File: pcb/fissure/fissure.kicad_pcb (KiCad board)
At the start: 2 copper layers, 151.2 x 81.6 mm, 84 parts, among them J1 AudioJack4, J2 AudioJack4, J3 Conn_01x08, J4 Conn_01x08, J5 Conn_01x08, J6 Conn_01x08, J9 Conn_01x04, K1 KEYSW, K10 KEYSW, K11 KEYSW, K12 KEYSW, K13 KEYSW, K14 KEYSW, K15 KEYSW, K16 KEYSW, K17 KEYSW, K18 KEYSW, K19 KEYSW, K2 KEYSW, K20 KEYSW, K3 KEYSW, K4 KEYSW, K5 KEYSW, K6 KEYSW, K7 KEYSW, K8 KEYSW, K9 KEYSW, SW1 SW_PUSH, SW2 SW_PUSH, U1 ProMicro, U2 MT25QL128ABA1ESE

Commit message: Clean up design files
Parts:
- D1, D10, D11, D12, D13, D14, D15, D16, D17, D18, D19, D2, D20, D21, D22, D23, D24, D25, D26, D27, D28, D29, D3, D30, D31, D32, D33, D34, D35, D36, D37, D38, D39, D4, D40, D5, D6, D7, D8, D9: value DIODE -> D
- J5: renamed from J9; value Conn_01x04 -> OLED
- K1, K10, K11, K12, K13, K14, K15, K16, K17, K18, K19, K2, K20, K3, K4, K5, K6, K7, K8, K9: value KEYSW -> SW_Push
- R1, R2: value R -> 4.7k
- R3: value R -> 10k
- SW1, SW2: value SW_PUSH -> SW_Push
- renumbered J4 to J3, J6 to J4, J3 to J6, J5 to J7
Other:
- outline, holes or cut-outs redrawn

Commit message: update pcb
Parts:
- removed J1: AudioJack4, Keebio-Parts:TRRS-PJ-320D
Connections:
- J4 pad 5: Net-(J4-Pad5) -> bridge_SCL
- J4 pad 6: Net-(J4-Pad6) -> bridge_SDA
- J4 pad 7: Net-(J4-Pad7) -> bridge_VCC
- J4 pad 8: Net-(J4-Pad8) -> bridge_GND
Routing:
- net bridge_GND: track 62.2 -> 72.5 mm
- net bridge_SCL: track 61.7 -> 67.1 mm
- net bridge_SDA: track 62.9 -> 64.5 mm, vias 2 -> 1
- net Net-(J3-Pad2): track 27.6 -> 29.1 mm
- net Net-(J3-Pad3): track 34.0 -> 35.0 mm
- net bridge_VCC: vias 2 -> 1

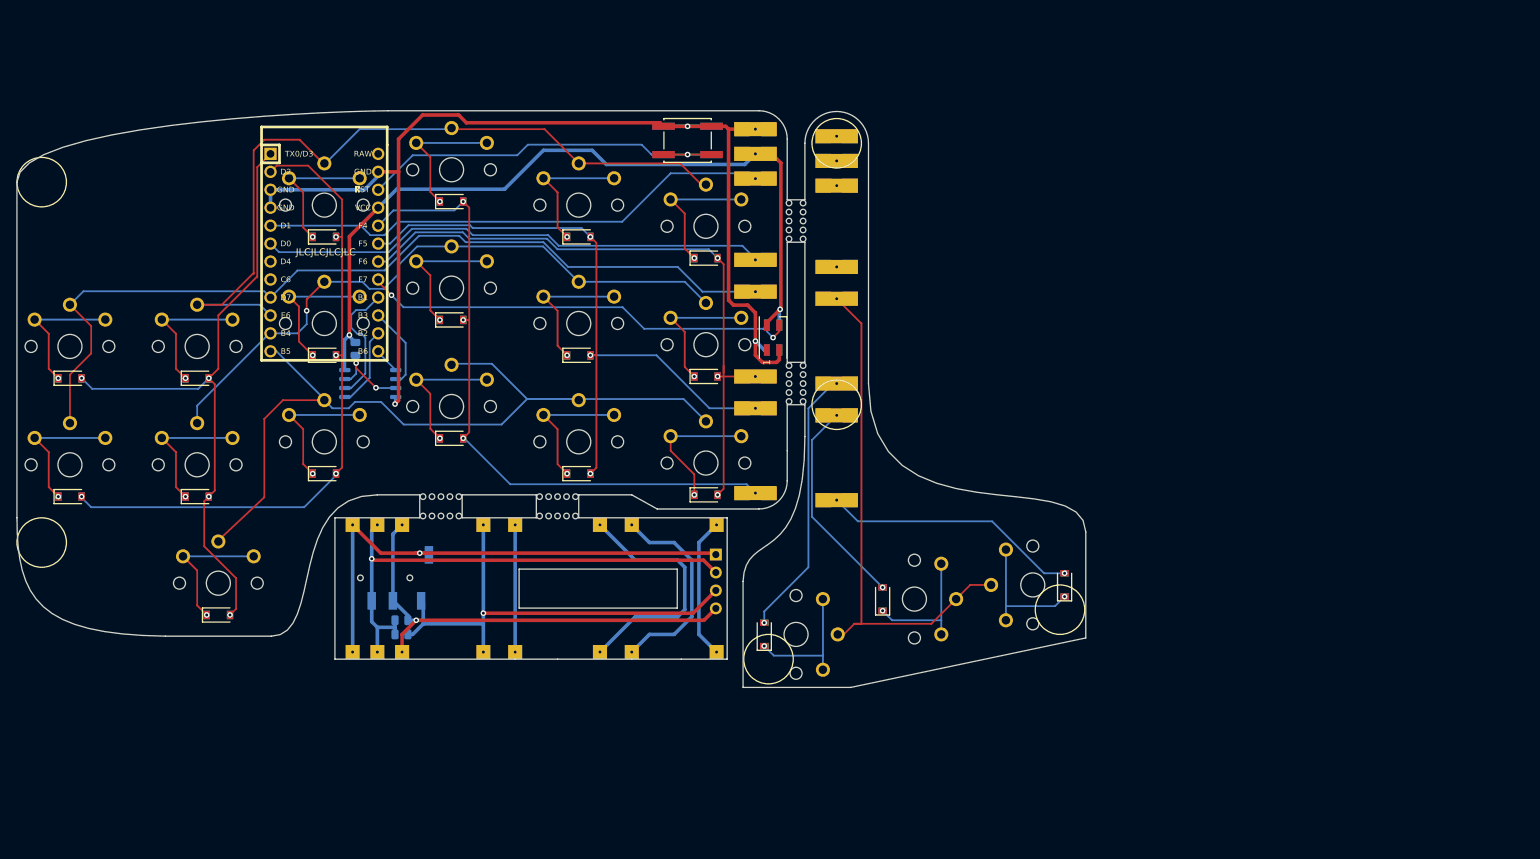
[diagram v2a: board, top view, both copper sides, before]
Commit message: Use new switch footprint
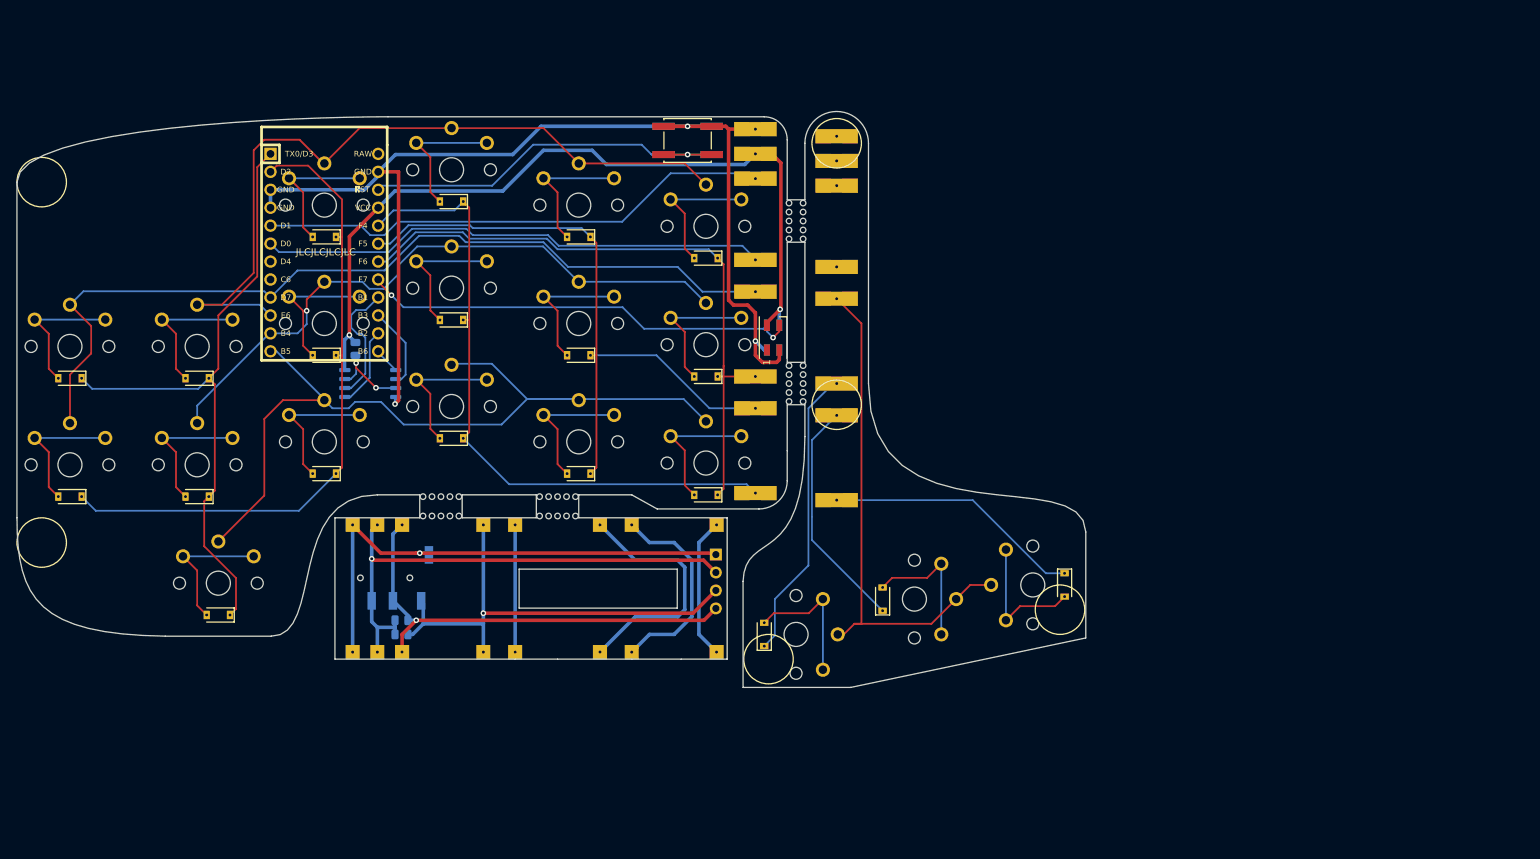
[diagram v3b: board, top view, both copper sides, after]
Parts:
- removed D1, D10, D11, D12, D13, D14, D15, D16, D17, D18, D19, D2, D20, D21, D22, D23, D24, D25, D26, D27, D28, D29, D3, D30, D31, D32, D33, D34, D35, D36, D37, D38, D39, D4, D40, D5, D6, D7, D8, D9: D, Diode_SMD:D_SOD-123
- K1, K10, K11, K12, K13, K14, K15, K16, K17, K2, K3, K4, K5, K6, K7, K8, K9: value SW_Push -> PG1350; footprint Keebio-Parts:Kailh-PG1350-1u-reversible-No-Clickhole -> pg1350:PG1350-reversible-rev
- K18, K19, K20: value SW_Push -> PG1350; footprint Keebio-Parts:Kailh-PG1350-1u-reversible-No-Clickhole -> pg1350:PG1350-reversible-rev; moved to F.Cu
- moved K1 4.50 mm to (51.5, 92.2), turned to 0 degrees
- moved K10 4.50 mm to (123.5, 92.0), turned to 0 degrees
- moved K11 4.50 mm to (54.5, 125.8), turned to 0 degrees
- moved K12 4.50 mm to (69.5, 105.8), turned to 0 degrees
- moved K13 4.50 mm to (87.5, 100.8), turned to 0 degrees
- moved K14 4.50 mm to (105.5, 105.8), turned to 0 degrees
- moved K15 4.50 mm to (123.5, 108.8), turned to 0 degrees
- moved K16 4.50 mm to (33.5, 92.2), turned to 0 degrees
- moved K17 4.50 mm to (33.5, 109.0), turned to 0 degrees
- moved K18 4.50 mm to (174.2, 121.5)
- moved K19 4.50 mm to (148.5, 123.5)
- moved K2 4.50 mm to (69.5, 72.2), turned to 0 degrees
- moved K20 4.50 mm to (131.8, 128.5)
- moved K3 4.50 mm to (87.5, 67.2), turned to 0 degrees
- moved K4 4.50 mm to (105.5, 72.2), turned to 0 degrees
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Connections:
- K1 pad 2: Net-(D1-Pad1) -> COL1
- K10 pad 2: Net-(D19-Pad1) -> COL5
- K11 pad 2: Net-(D21-Pad1) -> COL1
- K12 pad 2: Net-(D23-Pad1) -> COL2
- K13 pad 2: Net-(D25-Pad1) -> COL3
- K14 pad 2: Net-(D27-Pad1) -> COL4
- K15 pad 2: Net-(D29-Pad1) -> COL5
- K16 pad 2: Net-(D31-Pad1) -> COL1
- K17 pad 2: Net-(D33-Pad1) -> COL2
- K18 pad 2: Net-(D35-Pad1) -> thumb_COL3
- K19 pad 2: Net-(D37-Pad1) -> thumb_COL4
- K2 pad 2: Net-(D3-Pad1) -> COL2
- K20 pad 2: Net-(D39-Pad1) -> thumb_COL5
- K3 pad 2: Net-(D5-Pad1) -> COL3
- K4 pad 2: Net-(D7-Pad1) -> COL4
- K5 pad 2: Net-(D10-Pad1) -> COL5
- K6 pad 2: Net-(D11-Pad1) -> COL1
- K7 pad 2: Net-(D13-Pad1) -> COL2
- K8 pad 2: Net-(D15-Pad1) -> COL3
- K9 pad 2: Net-(D17-Pad1) -> COL4
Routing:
- net Net-(D33-Pad1): track 19.7 -> 0.00 mm, vias 1 -> 0
- net Net-(D31-Pad1): track 19.7 -> 0.00 mm, vias 1 -> 0
- net Net-(D21-Pad1): track 19.7 -> 0.00 mm, vias 1 -> 0
- net Net-(D11-Pad1): track 19.7 -> 0.00 mm, vias 1 -> 0
- net Net-(D1-Pad1): track 19.7 -> 0.00 mm, vias 1 -> 0
- net Net-(D7-Pad1): track 19.7 -> 0.00 mm, vias 1 -> 0
- net Net-(D5-Pad1): track 19.7 -> 0.00 mm, vias 1 -> 0
- net Net-(D3-Pad1): track 19.7 -> 0.00 mm, vias 1 -> 0
- net Net-(D29-Pad1): track 19.7 -> 0.00 mm, vias 1 -> 0
- net Net-(D27-Pad1): track 19.7 -> 0.00 mm, vias 1 -> 0
- net Net-(D25-Pad1): track 19.7 -> 0.00 mm, vias 1 -> 0
- net Net-(D23-Pad1): track 19.7 -> 0.00 mm, vias 1 -> 0
- net Net-(D19-Pad1): track 19.7 -> 0.00 mm, vias 1 -> 0
- net Net-(D17-Pad1): track 19.7 -> 0.00 mm, vias 1 -> 0
- net Net-(D15-Pad1): track 19.7 -> 0.00 mm, vias 1 -> 0
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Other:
- board size 151.2 x 81.6 mm -> 151.2 x 81.5 mm

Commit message: Use holyiot 18010 + USB C
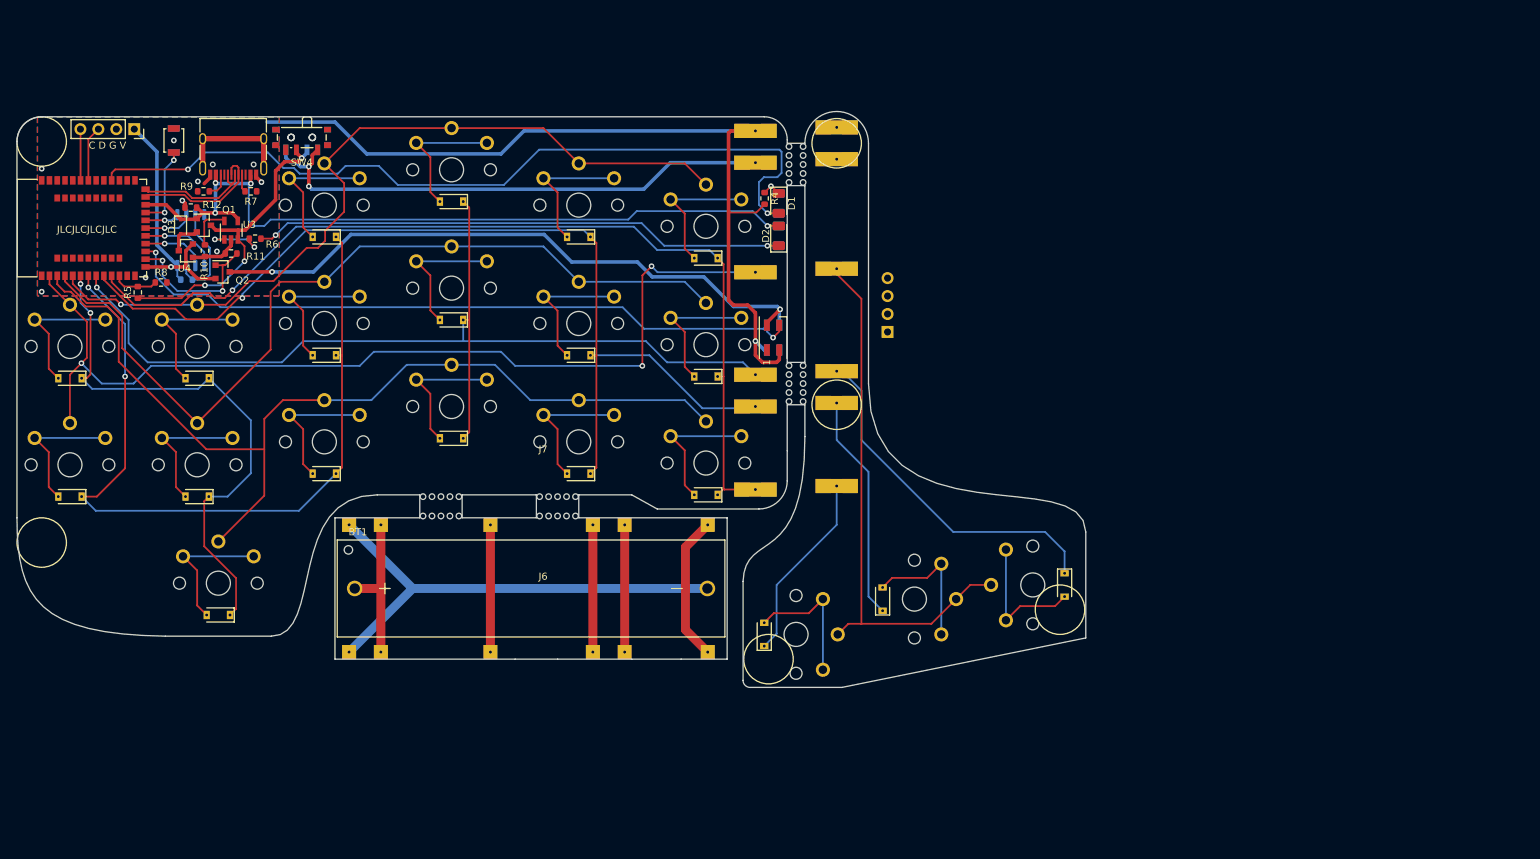
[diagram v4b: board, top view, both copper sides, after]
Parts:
- removed R1, R2: 4.7k, Resistor_SMD:R_0805_2012Metric
- removed the REF** at (137.5, 70.0)
- removed the REF** at (135.0, 70.0)
- added BT1: Battery_Cell, misc:BA1AAAPC, F.Cu at (98.8, 122.0)
- added D1: BLUE, LED_SMD:LED_1206_3216Metric, F.Cu at (133.8, 67.5)
- added D2: RED, LED_SMD:LED_1206_3216Metric, F.Cu at (133.8, 72.1)
- added D3: 1N5819, Diode_SMD:D_SOD-323, F.Cu at (49.1, 70.8)
- added D4: BLUE, LED_SMD:LED_1206_3216Metric, B.Cu at (133.8, 67.5)
- added D5: RED, LED_SMD:LED_1206_3216Metric, B.Cu at (133.8, 72.1)
- added J1: Conn_01x04_Female, Connector_PinSocket_2.54mm:PinSocket_1x04_P2.54mm_Vertical, F.Cu at (42.6, 57.0)
- added Q1: AO3401A, Package_TO_SOT_SMD:SOT-23, F.Cu at (52.5, 70.6)
- added Q2: AO3401A, Package_TO_SOT_SMD:SOT-23, F.Cu at (55.1, 77.2)
- added R10: 10k, Resistor_SMD:R_0603_1608Metric, F.Cu at (52.6, 74.2)
- added R11: 2M, Resistor_SMD:R_0603_1608Metric, F.Cu at (56.3, 74.6)
- added R12: 100k, Resistor_SMD:R_0603_1608Metric, F.Cu at (50.6, 68.1)
- added R4: 1k, Resistor_SMD:R_0603_1608Metric, F.Cu at (131.8, 66.8)
- added R5: 820k, Resistor_SMD:R_0603_1608Metric, F.Cu at (43.1, 80.1)
- added R6: 1k, Resistor_SMD:R_0603_1608Metric, F.Cu at (59.7, 72.5)
- added R7: 5.1k, Resistor_SMD:R_0603_1608Metric, F.Cu at (59.1, 65.8)
- added R8: 2M, Resistor_SMD:R_0603_1608Metric, F.Cu at (46.4, 78.7)
- added R9: 5.1k, Resistor_SMD:R_0603_1608Metric, F.Cu at (52.4, 65.8)
- added REF**: breakaway-mousebites, Keebio-Parts:breakaway-mousebites, F.Cu at (137.5, 62.0)
- added REF**: breakaway-mousebites, Keebio-Parts:breakaway-mousebites, F.Cu at (135.0, 62.0)
- added SW3: SW_SPDT, Button_Switch_SMD:SW_SPDT_PCM12, B.Cu at (66.3, 58.5)
- added SW4: SW_SPDT, Button_Switch_SMD:SW_SPDT_PCM12, F.Cu at (66.3, 58.5)
- added U3: LTC4054ES5-4.2, Package_TO_SOT_SMD:TSOT-23-5, F.Cu at (56.3, 71.3)
- added U4: MCP1700-3302E_SOT23, Package_TO_SOT_SMD:SOT-23, F.Cu at (49.9, 74.2)
- J2: value AudioJack4 -> USB_C_Receptacle_USB2.0; footprint Keebio-Parts:TRRS-PJ-320D -> Connector_USB:USB_C_Receptacle_HRO_TYPE-C-31-M-12; moved to F.Cu
- J3, J4: value Conn_01x08 -> Conn_01x06; footprint fissure:bridge -> fissure:bridge-conn
- J5: footprint steno:OLED -> misc:OLED
- J6: value Conn_01x08 -> Conn_01x06; footprint fissure:bridge-conn -> fissure:bridge
- J7: value Conn_01x08 -> Conn_01x06; footprint fissure:bridge-conn -> fissure:bridge; moved to F.Cu
- R3: footprint Resistor_SMD:R_0805_2012Metric -> Resistor_SMD:R_0603_1608Metric
- SW1, SW2: footprint Button_Switch_SMD:SW_SPST_EVQQ2 -> Button_Switch_SMD:SW_SPST_B3U-1000P
- U1: value ProMicro -> Holyiot_18010; footprint Keebio-Parts:ArduinoProMicro -> misc:Holyiot_18010
- moved SW1 72.7 mm to (48.2, 58.6), turned to 90 degrees
- moved SW2 72.7 mm to (48.2, 58.6), turned to 90 degrees
- moved J2 63.3 mm to (56.6, 59.4), turned to 180 degrees
- moved J6 55.5 mm to (100.2, 131.0), turned to 180 degrees
- moved J5 55.3 mm to (147.6, 75.9), turned to 0 degrees
- moved J3 55.1 mm to (130.5, 84.5), turned to 90 degrees
- moved J4 50.2 mm to (142.0, 84.0), turned to 90 degrees
- moved J7 50.0 mm to (100.2, 113.0), turned to 180 degrees
- moved U1 34.5 mm to (35.2, 71.0), turned to 90 degrees
- moved U2 32.5 mm to (50.6, 72.7), turned to 270 degrees
- moved R3 25.8 mm to (50.0, 78.3), turned to 0 degrees
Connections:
- net RAW renamed Net-(U1-Pad24)
- D41 pad 4: VCC -> EXT_VCC
- D42 pad 4: VCC -> EXT_VCC
- J3 pad 1: Net-(J3-Pad1) -> GND
- J3 pad 2: Net-(J3-Pad2) -> BAT
- J3 pad 3: Net-(J3-Pad3) -> ROW4
- J3 pad 4: Net-(J3-Pad4) -> COL3
- J3 pad 5: bridge_SCL -> COL4
- J3 pad 6: bridge_SDA -> COL5
- J4 pad 1: Net-(J3-Pad1) -> thumb_GND
- J4 pad 2: Net-(J3-Pad2) -> thumb_BAT
- J4 pad 3: Net-(J3-Pad3) -> thumb_ROW4
- J4 pad 4: Net-(J3-Pad4) -> thumb_COL3
- J4 pad 5: bridge_SCL -> thumb_COL4
- J4 pad 6: bridge_SDA -> thumb_COL5
- J5 pad 1: bridge_GND -> GND
- J5 pad 2: bridge_VCC -> EXT_VCC
- J5 pad 3: bridge_SCL -> SCL
- J5 pad 4: bridge_SDA -> SDA
- J6 pad 1: COL3 -> bridge_GND
- J6 pad 2: COL4 -> bridge_BAT
- J6 pad 3: COL5 -> Net-(J6-Pad3)
- J6 pad 4: ROW4 -> Net-(J6-Pad4)
- J6 pad 5: SCL -> Net-(J6-Pad5)
- J6 pad 6: SDA -> Net-(J6-Pad6)
- J7 pad 1: thumb_COL3 -> bridge_GND
- J7 pad 2: thumb_COL4 -> bridge_BAT
- J7 pad 3: thumb_COL5 -> Net-(J6-Pad3)
- J7 pad 4: thumb_ROW4 -> Net-(J6-Pad4)
- J7 pad 5: thumb_SCL -> Net-(J6-Pad5)
- J7 pad 6: thumb_SDA -> Net-(J6-Pad6)
- R3 pad 1: VCC -> VDD
- U1 pad 1: COL1 -> GND
- U1 pad 10: ROW1 -> COL5
- U1 pad 11: ROW2 -> BAT_MEAS
- U1 pad 12: ROW3 -> Net-(U1-Pad12)
- U1 pad 13: CS -> Net-(U1-Pad13)
- U1 pad 14: MOSI_DQ0 -> Net-(U1-Pad14)
- U1 pad 15: MISO_DQ1 -> Net-(U1-Pad15)
- U1 pad 16: SCLK -> Net-(U1-Pad16)
- U1 pad 17: RGB -> Net-(U1-Pad17)
- U1 pad 18: COL5 -> Net-(U1-Pad18)
- U1 pad 19: COL4 -> Net-(U1-Pad19)
- U1 pad 2: COL2 -> ROW4
- U1 pad 20: COL3 -> Net-(U1-Pad20)
- U1 pad 21: VCC -> Net-(U1-Pad21)
- U1 pad 22: RST -> Net-(U1-Pad22)
- U1 pad 23: GND -> Net-(U1-Pad23)
- U1 pad 3: GND -> ROW3
- U1 pad 4: GND -> ROW2
- U1 pad 5: SDA -> ROW1
- U1 pad 6: SCL -> COL1
- U1 pad 7: Net-(U1-Pad7) -> COL2
- U1 pad 8: Net-(U1-Pad8) -> COL3
- U1 pad 9: ROW4 -> COL4
- U2 pad 8: VCC -> VDD
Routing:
- net BLUE: track 0.00 -> 116.9 mm, vias 0 -> 2
- net VCC: track 115.1 -> 0.00 mm, vias 2 -> 0
- net VBUS: track 0.00 -> 111.9 mm, vias 0 -> 4
- net EXT_VCC: track 0.00 -> 90.2 mm, vias 0 -> 2
- net Net-(D2-Pad1): track 0.00 -> 77.1 mm, vias 0 -> 2
- net BAT: track 0.00 -> 75.5 mm, vias 0 -> 2
- net SDA: track 73.3 -> 0.00 mm
- net bridge_VCC: track 72.9 -> 0.00 mm, vias 1 -> 0
- net SCL: track 72.2 -> 0.00 mm
- net bridge_SCL: track 67.1 -> 0.00 mm, vias 1 -> 0
- net bridge_SDA: track 64.5 -> 0.00 mm, vias 1 -> 0
- net COL3: track 93.1 -> 142.5 mm, vias 0 -> 1
- net COL4: track 93.3 -> 139.2 mm, vias 0 -> 1
- net MCU_BAT: track 0.00 -> 44.8 mm, vias 0 -> 3
- net COL5: track 91.8 -> 136.4 mm, vias 0 -> 1
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- added copper zone on B.Cu, net GND
- added copper zone on F.Cu, net GND
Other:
- outline, holes or cut-outs redrawn
- net class Default: clearance 0.2 -> 0.2032; trace_width 0.25 -> 0.254
- rule trace_clearance: 0.2 -> 0.2032
- board text added: "C D G V"
- board text added: "V G D C"
- board text removed: "4.7k"
